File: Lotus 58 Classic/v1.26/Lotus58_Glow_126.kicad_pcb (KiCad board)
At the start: 2 copper layers, 139.1 x 107.7 mm, 125 parts, among them J1 PJ-320A, J2 Conn_01x02, P1 OLED, SW1 Kailh hotswap MX socket, SW10 Kailh hotswap MX socket, SW11 Kailh hotswap MX socket, SW12 Kailh hotswap MX socket, SW13 Kailh hotswap MX socket, SW14 Kailh hotswap MX socket, SW15 Kailh hotswap MX socket, SW16 Kailh hotswap MX socket, SW17 Kailh hotswap MX socket, SW18 Kailh hotswap MX socket, SW19 Kailh hotswap MX socket, SW2 Kailh hotswap MX socket, SW20 Kailh hotswap MX socket, SW21 Kailh hotswap MX socket, SW22 Kailh hotswap MX socket, SW23 Kailh hotswap MX socket, SW24 Kailh hotswap MX socket, SW25 Kailh hotswap MX socket, SW26 Kailh hotswap MX socket, SW27 Kailh hotswap MX socket, SW28 Kailh hotswap MX socket, SW29 Kailh hotswap MX socket, SW3 Kailh hotswap MX socket, SW30 Rotary_Encoder_Switch, SW31 Rotary_Encoder_Switch, SW4 Kailh hotswap MX socket, SW5 Kailh hotswap MX socket, SW6 Kailh hotswap MX socket, SW7 Kailh hotswap MX socket, SW8 Kailh hotswap MX socket, SW9 Kailh hotswap MX socket, U1 ProMicro, U2 SRV05-4

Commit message: v1.26 final
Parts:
- removed JP1, JP4: RESET, Common Library:Jumper_Mini
- added RES1: TS-A002, Keyboard Common:YTS-A002, B.Cu at (118.9, 37.2)
- added RES2: TS-A002, Keyboard Common:YTS-A002, F.Cu at (118.9, 37.2)
- added S2: MSK12C02, Keyboard Common:MSK12C02, B.Cu at (108.7, 37.5)
- added S3: MSK12C02, Keyboard Common:MSK12C02, F.Cu at (103.1, 94.5)
- LED1, LED2, LED3, LED5, LED6: moved to B.Cu
- SW1, SW10, SW11, SW12, SW13, SW14, SW15, SW16, SW17, SW18, SW19, SW2, SW20, SW21, SW22, SW23, SW24, SW25, SW26, SW27, SW28, SW29, SW3, SW4, SW5, SW6, SW7, SW8, SW9: footprint keyswitches:Kailh_socket_MX_reversible_RGB -> Keyboard Switches:SW_MX_HotSwap_Reversible; moved to B.Cu
- moved Logo2 38.0 mm to (64.8, 87.0)
- moved JP5 6.29 mm to (101.6, 87.1), turned to 0 degrees
- moved JP6 5.48 mm to (101.6, 85.4), turned to 0 degrees
- moved S1 2.99 mm to (108.7, 37.5)
- moved D1 0.26 mm to (114.5, 41.7)
- turned SW1 to 180 degrees
- turned SW10 to 180 degrees
- turned SW11 to 180 degrees
- turned SW12 to 180 degrees
- turned SW13 to 180 degrees
- turned SW14 to 180 degrees
- turned SW15 to 180 degrees
- turned SW16 to 180 degrees
- turned SW17 to 180 degrees
- turned SW18 to 180 degrees
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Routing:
- net RESET: track 26.4 -> 48.1 mm, vias 2 -> 4
- net col1: track 238.7 -> 257.1 mm
- net Battery: track 20.2 -> 28.9 mm, vias 0 -> 2
- net /PWR_GLOW: track 301.3 -> 309.5 mm
- net /PWR_KEY: track 695.7 -> 703.8 mm, vias 36 -> 38
- net GND: track 179.8 -> 186.9 mm, vias 89 -> 101
- net VCC: track 93.3 -> 97.3 mm
- net /Batt: track 6.11 -> 8.89 mm, vias 0 -> 1
- net col4: track 180.9 -> 183.3 mm
- net col2: track 220.2 -> 221.8 mm
- net col0: track 213.7 -> 214.9 mm
- net Net-(D26-A): track 9.41 -> 10.4 mm
- net Alt: track 16.5 -> 15.8 mm
- net Net-(LED2-DOUT): track 44.7 -> 45.4 mm
- net Net-(LED23-DOUT): track 20.7 -> 21.3 mm
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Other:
- board text removed: "RESET"

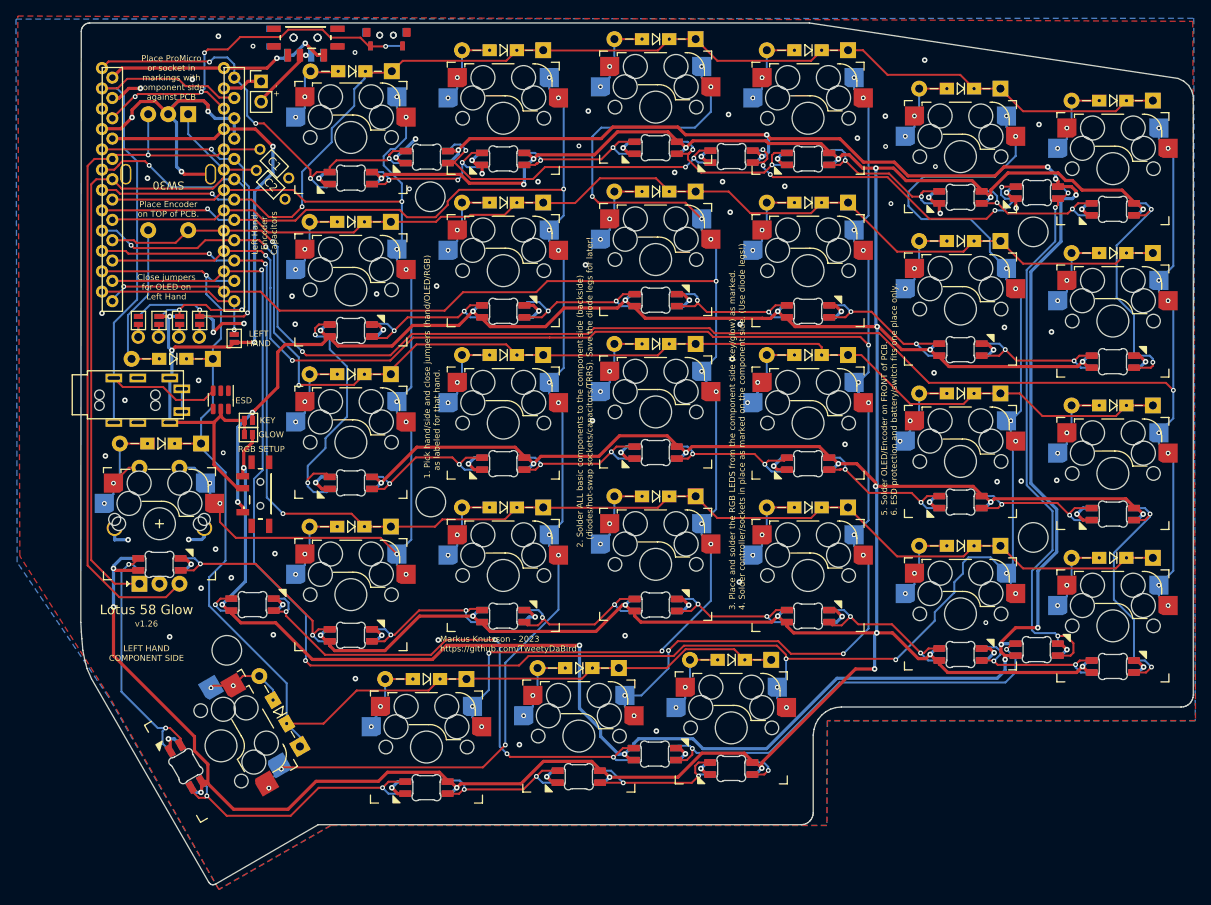
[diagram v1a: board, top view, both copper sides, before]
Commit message: Fixed silk screen inconsistencies
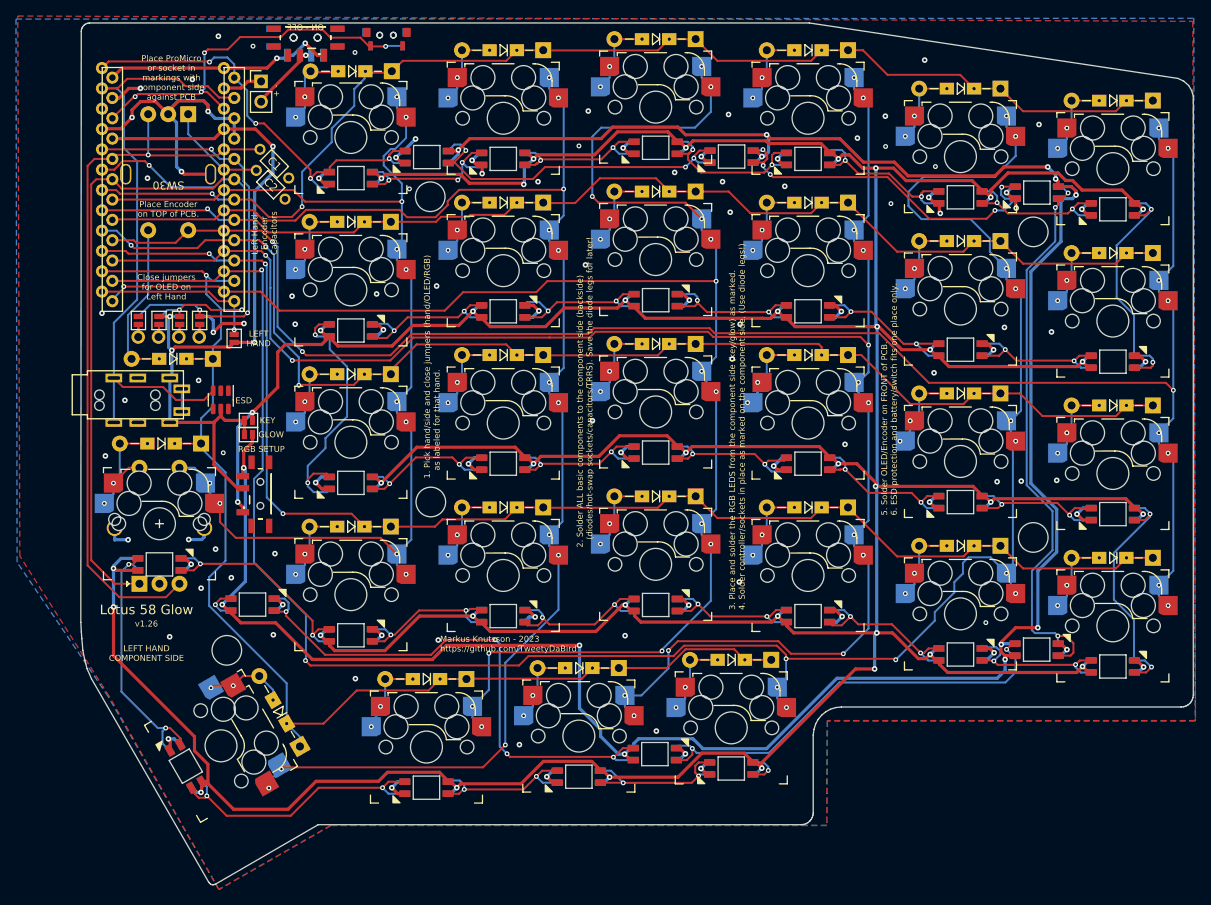
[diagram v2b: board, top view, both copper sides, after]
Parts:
- moved Logo2 134.8 mm to (199.4, 79.6)
